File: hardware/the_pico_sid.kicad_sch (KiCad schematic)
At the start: 18 parts, among them J1 SWD, U1 4050, U2 SID_6581, U3 4050, U4 4050, U5 Pico

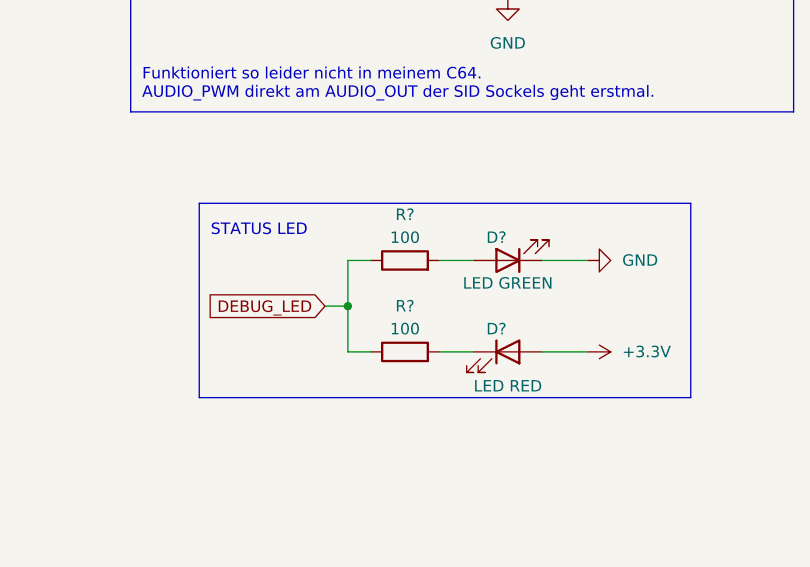
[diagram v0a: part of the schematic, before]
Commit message: sheamtic: changed debug  led's resitors from 100 to 200 ohm
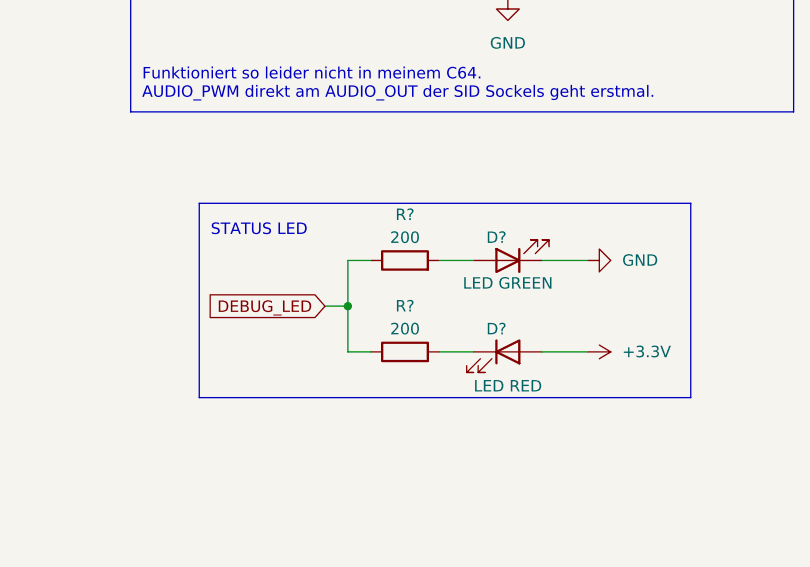
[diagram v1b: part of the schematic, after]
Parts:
- R? (x2): value 100 -> 200
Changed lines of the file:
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@@
     (in_bom yes) (on_board yes)
     (property "Reference" "R?" (id 0) (at 220.98 78.74 90))
-    (property "Value" "100" (id 1) (at 220.98 81.28 90))
+    (property "Value" "200" (id 1) (at 220.98 81.28 90))
     (property "Footprint" "" (id 2) (at 220.98 85.598 90)
       (effects (font (size 1.27 1.27)) hide)
@@
     (in_bom yes) (on_board yes)
     (property "Reference" "R?" (id 0) (at 220.98 88.9 90))
-    (property "Value" "100" (id 1) (at 220.98 91.44 90))
+    (property "Value" "200" (id 1) (at 220.98 91.44 90))
     (property "Footprint" "" (id 2) (at 220.98 95.758 90)
       (effects (font (size 1.27 1.27)) hide)
@@
     )
     (path "/3923cd97-749d-4518-818c-7cf624d0e03f"
-      (reference "R?") (unit 1) (value "100") (footprint "")
+      (reference "R?") (unit 1) (value "200") (footprint "")
     )
     (path "/c0bee8e1-2c4b-4de5-9f03-97b8cfd8792f"
-      (reference "R?") (unit 1) (value "100") (footprint "")
+      (reference "R?") (unit 1) (value "200") (footprint "")
     )
     (path "/9dc66f85-19b8-4dfd-859b-d40546c9d1c1"

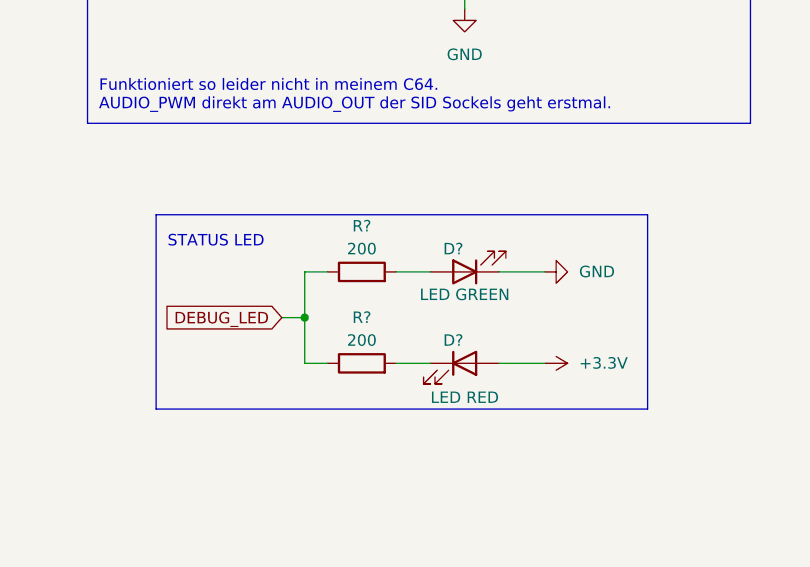
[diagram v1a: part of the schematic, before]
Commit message: schematic: led resitors from 200 to 1k ohm
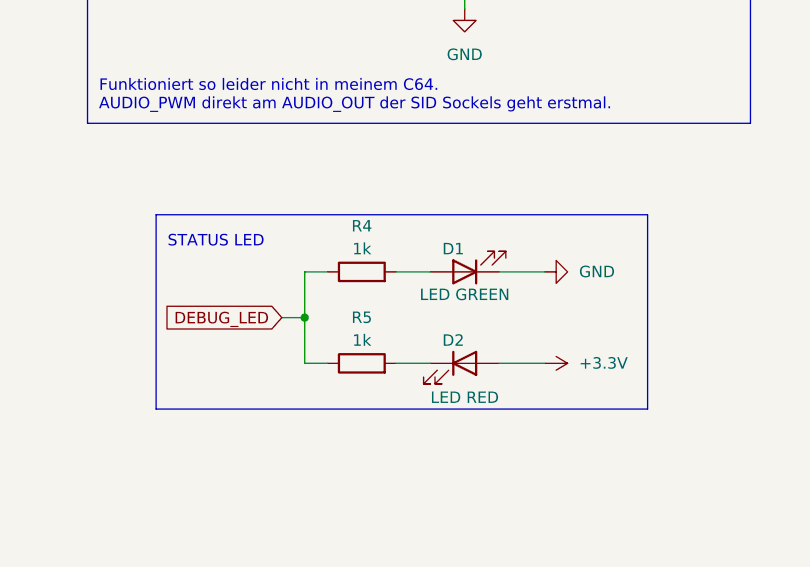
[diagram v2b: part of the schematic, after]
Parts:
- R4, R5: renamed from R?; value 200 -> 1k
- gave numbers to parts that had none: 2
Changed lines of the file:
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@@
   (symbol (lib_id "power:+3.3V") (at 241.3 93.98 270) (unit 1)
     (in_bom yes) (on_board yes) (fields_autoplaced)
-    (property "Reference" "#PWR?" (id 0) (at 237.49 93.98 0)
+    (property "Reference" "#PWR017" (id 0) (at 237.49 93.98 0)
       (effects (font (size 1.27 1.27)) hide)
     )
@@
   (symbol (lib_id "Device:R") (at 220.98 83.82 90) (unit 1)
     (in_bom yes) (on_board yes)
-    (property "Reference" "R?" (id 0) (at 220.98 78.74 90))
-    (property "Value" "200" (id 1) (at 220.98 81.28 90))
+    (property "Reference" "R4" (id 0) (at 220.98 78.74 90))
+    (property "Value" "1k" (id 1) (at 220.98 81.28 90))
     (property "Footprint" "" (id 2) (at 220.98 85.598 90)
       (effects (font (size 1.27 1.27)) hide)
@@
   (symbol (lib_id "Device:LED") (at 232.41 93.98 0) (unit 1)
     (in_bom yes) (on_board yes)
-    (property "Reference" "D?" (id 0) (at 231.14 91.44 0))
+    (property "Reference" "D2" (id 0) (at 231.14 91.44 0))
     (property "Value" "LED RED" (id 1) (at 232.41 97.79 0))
     (property "Footprint" "" (id 2) (at 232.41 93.98 0)
@@
   (symbol (lib_id "Device:LED") (at 232.41 83.82 180) (unit 1)
     (in_bom yes) (on_board yes)
-    (property "Reference" "D?" (id 0) (at 231.14 81.28 0))
+    (property "Reference" "D1" (id 0) (at 231.14 81.28 0))
     (property "Value" "LED GREEN" (id 1) (at 232.41 86.36 0))
     (property "Footprint" "" (id 2) (at 232.41 83.82 0)
@@
   (symbol (lib_id "Device:R") (at 220.98 93.98 90) (unit 1)
     (in_bom yes) (on_board yes)
-    (property "Reference" "R?" (id 0) (at 220.98 88.9 90))
-    (property "Value" "200" (id 1) (at 220.98 91.44 90))
+    (property "Reference" "R5" (id 0) (at 220.98 88.9 90))
+    (property "Value" "1k" (id 1) (at 220.98 91.44 90))
     (property "Footprint" "" (id 2) (at 220.98 95.758 90)
       (effects (font (size 1.27 1.27)) hide)
@@
   (symbol (lib_id "power:GND") (at 241.3 83.82 90) (unit 1)
     (in_bom yes) (on_board yes) (fields_autoplaced)
-    (property "Reference" "#PWR?" (id 0) (at 247.65 83.82 0)
+    (property "Reference" "#PWR016" (id 0) (at 247.65 83.82 0)
       (effects (font (size 1.27 1.27)) hide)
     )
@@
       (reference "#PWR015") (unit 1) (value "GND") (footprint "")
     )
+    (path "/e352f26a-cb5b-4fac-9ef1-af3a963faf9e"
+      (reference "#PWR016") (unit 1) (value "GND") (footprint "")
+    )
     (path "/0d4bf249-808f-48dc-94e5-ef9edca5058c"
-      (reference "#PWR?") (unit 1) (value "+3.3V") (footprint "")
-    )
-    (path "/e352f26a-cb5b-4fac-9ef1-af3a963faf9e"
-      (reference "#PWR?") (unit 1) (value "GND") (footprint "")
+      (reference "#PWR017") (unit 1) (value "+3.3V") (footprint "")
     )
     (path "/249fc3f4-6214-43d5-bed7-4570a982ba76"
@@
       (reference "C5") (unit 1) (value "100n") (footprint "")
     )
+    (path "/87a8def9-5869-4c5f-9ee6-703114a2517a"
+      (reference "D1") (unit 1) (value "LED GREEN") (footprint "")
+    )
     (path "/5e1f39e0-289e-4d8f-8733-aeb457bfcfdb"
-      (reference "D?") (unit 1) (value "LED RED") (footprint "")
-    )
-    (path "/87a8def9-5869-4c5f-9ee6-703114a2517a"
-      (reference "D?") (unit 1) (value "LED GREEN") (footprint "")
+      (reference "D2") (unit 1) (value "LED RED") (footprint "")
     )
     (path "/6d20c440-e8ae-442d-9b38-e1d32399f02f"
@@
     )
     (path "/3923cd97-749d-4518-818c-7cf624d0e03f"
-      (reference "R?") (unit 1) (value "200") (footprint "")
+      (reference "R4") (unit 1) (value "1k") (footprint "")
     )
     (path "/c0bee8e1-2c4b-4de5-9f03-97b8cfd8792f"
-      (reference "R?") (unit 1) (value "200") (footprint "")
+      (reference "R5") (unit 1) (value "1k") (footprint "")
     )
     (path "/9dc66f85-19b8-4dfd-859b-d40546c9d1c1"

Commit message: Update the_pico_sid.kicad_sch
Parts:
- removed C3: 100n, symbol Device:C
- removed C4: 47u, symbol Device:C_Polarized
- removed R1: 220, symbol Device:R
- removed R2: 100, symbol Device:R
- removed R3: 1,8k, symbol Device:R
- added C1: 100n, symbol Device:C
- added C2: 1u, symbol Device:C_Polarized
- added U1: TL084, symbol Amplifier_Operational:TL084
- renumbered C1 to C3, C2 to C4, R4 to R1, R5 to R2, U5 to U3, U1 to U4, U3 to U5, U4 to U6
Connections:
- net +5V: now also C1.1, U1.4 (V+)
- net AUDIO_OUT: now also U1.1, U1.2 (-)
- net AUDIO_PWM: now also C2.1
- net GND: now also C1.2, U1.11 (V-)
- new net: C2.2, U1.3 (+)
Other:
- note added: "Audio Out"
- note removed: "Audio Filter"
- note removed: "Funktioniert so leider nicht in meinem C64. AUDIO_PWM direkt am AUDIO_OUT der SID Sockels geht erstmal."

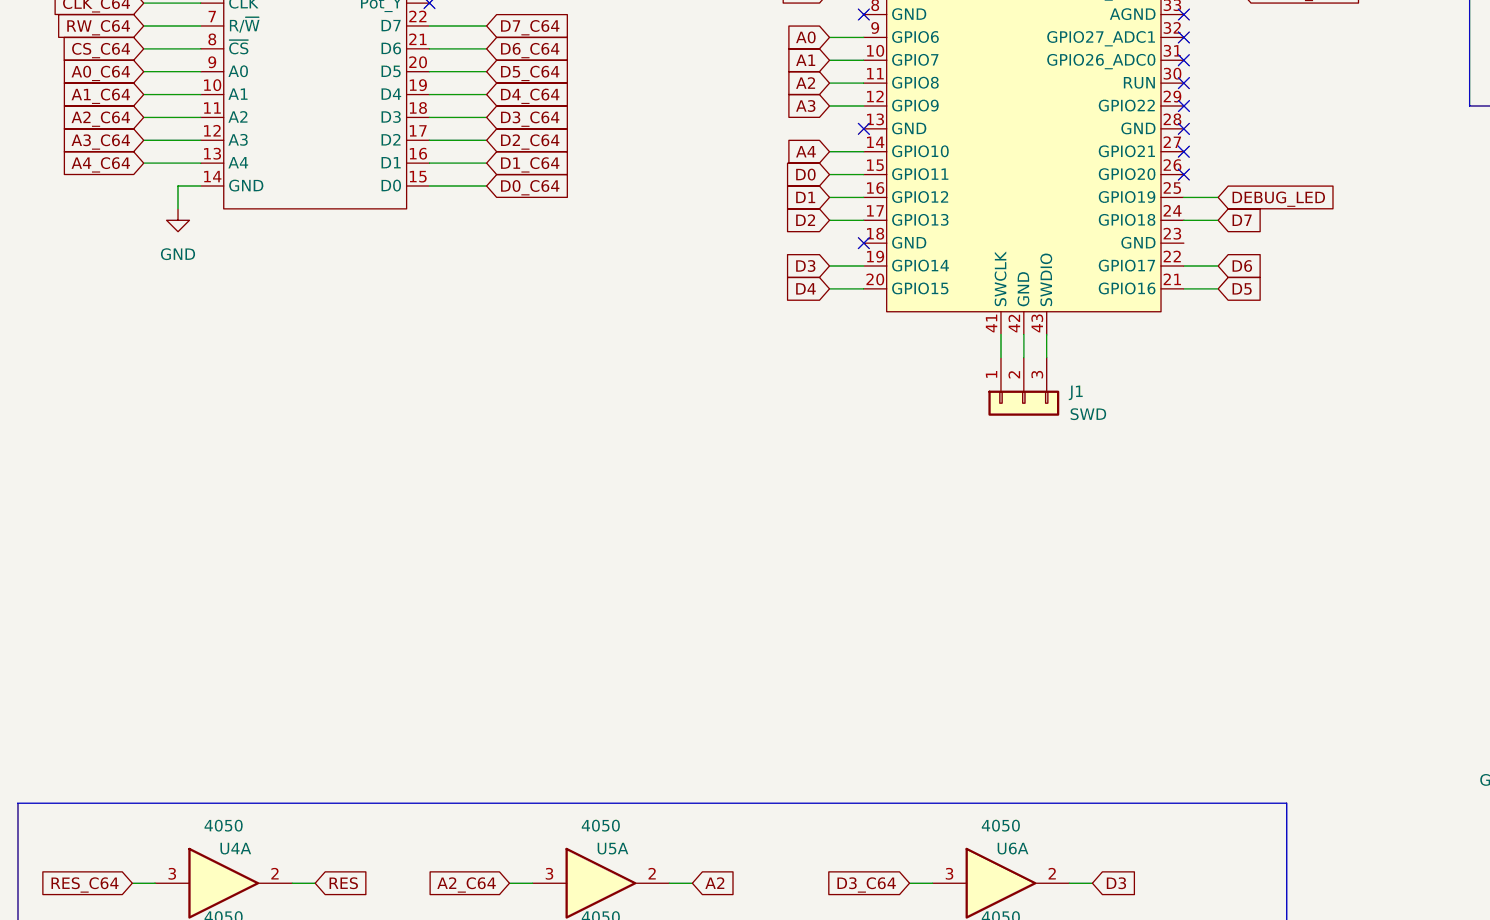
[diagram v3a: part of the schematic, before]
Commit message: schematic: added temporary ic 4520 counter
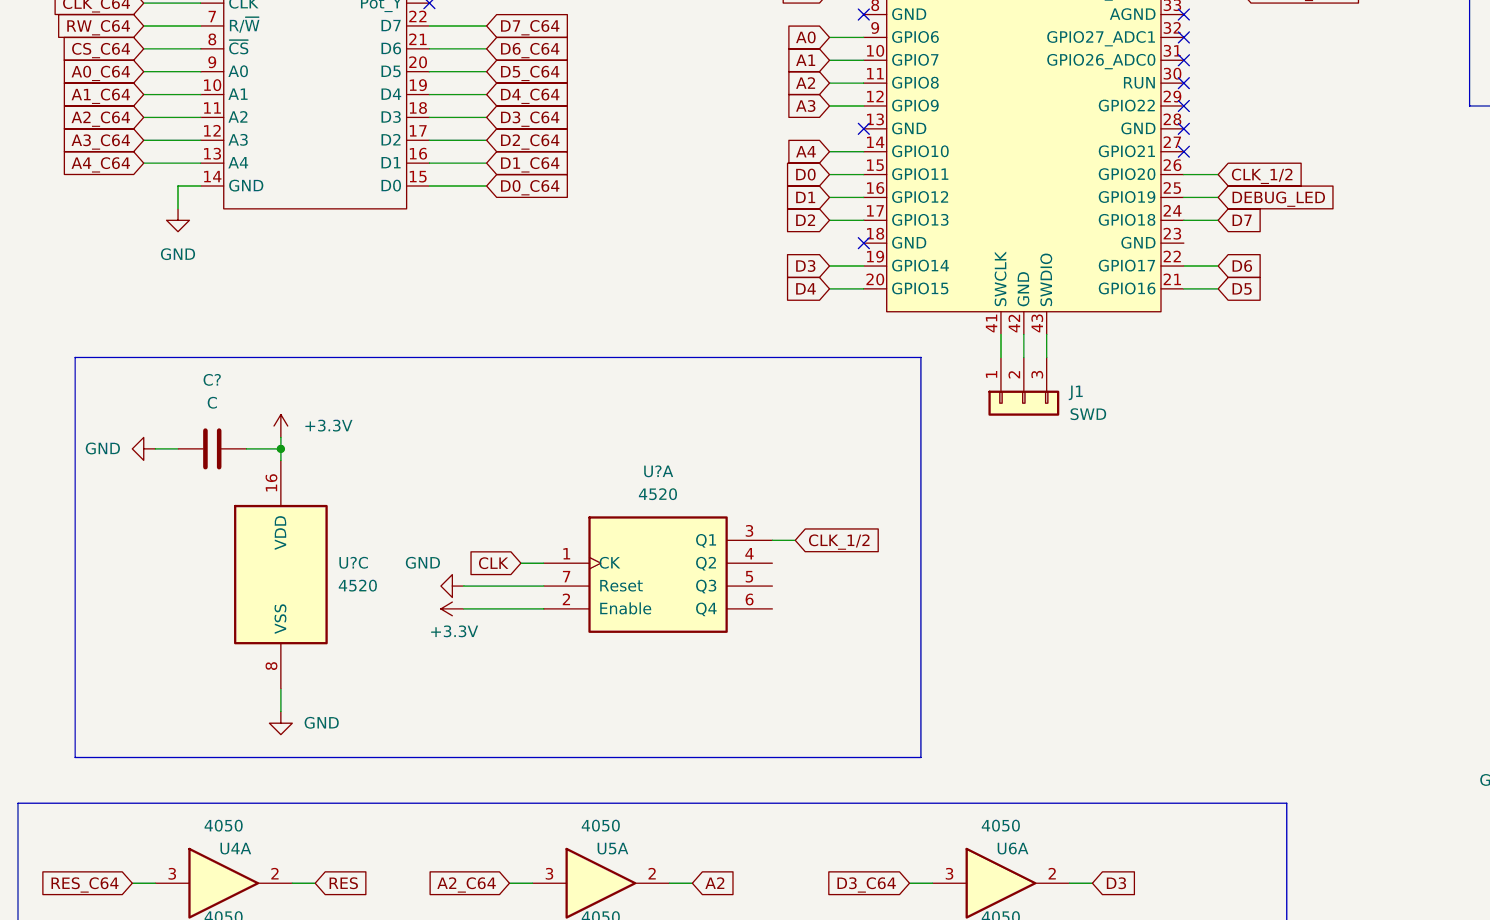
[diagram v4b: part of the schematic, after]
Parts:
- added C?: C, symbol Device:C
- added U? (x2): 4520, symbol 4xxx:4520
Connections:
- net +3.3V: now also C?.2, U?.16 (VDD), U?.2 (Enable)
- net CLK: now also U?.1 (CK)
- net GND: now also C?.1, U?.7 (Reset), U?.8 (VSS)
- net CLK_1/2: now reaches U3.26 (GPIO20)
- net CLK_1/2: now also U?.3 (Q1)
- no-connect marks 27 -> 26
